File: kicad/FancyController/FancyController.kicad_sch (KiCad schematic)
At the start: 9 parts, among them J3 ISP, U1 ATmega48-20P, U2 MAX232

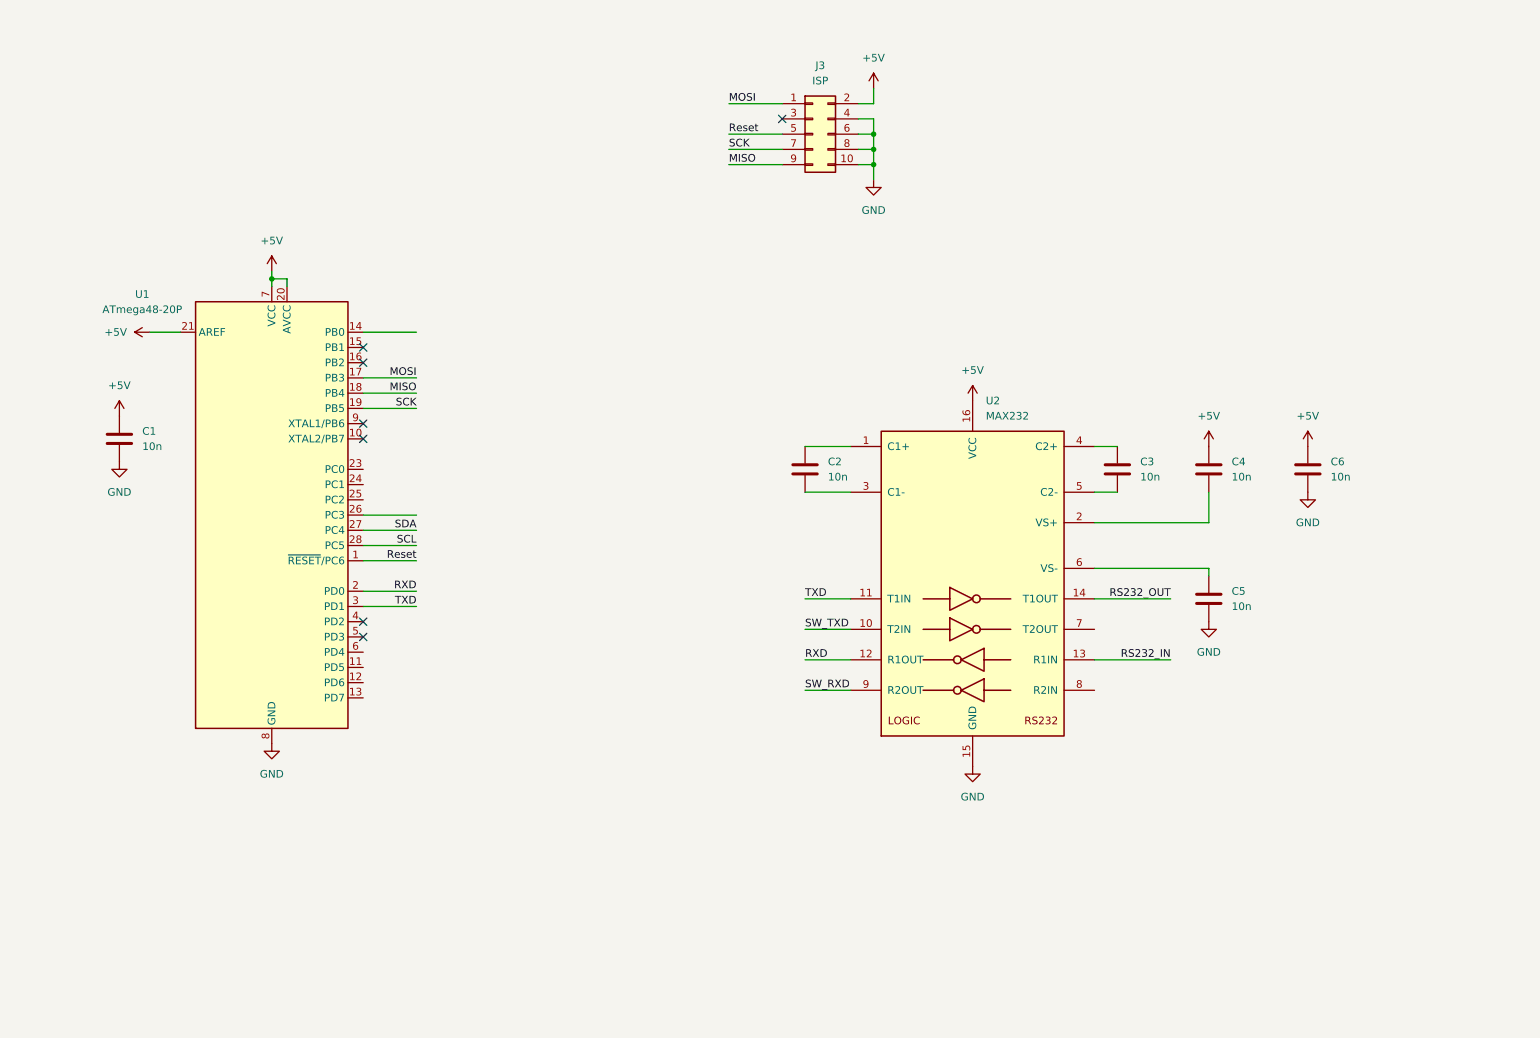
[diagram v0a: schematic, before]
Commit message: Complete schematics, using UART for communications
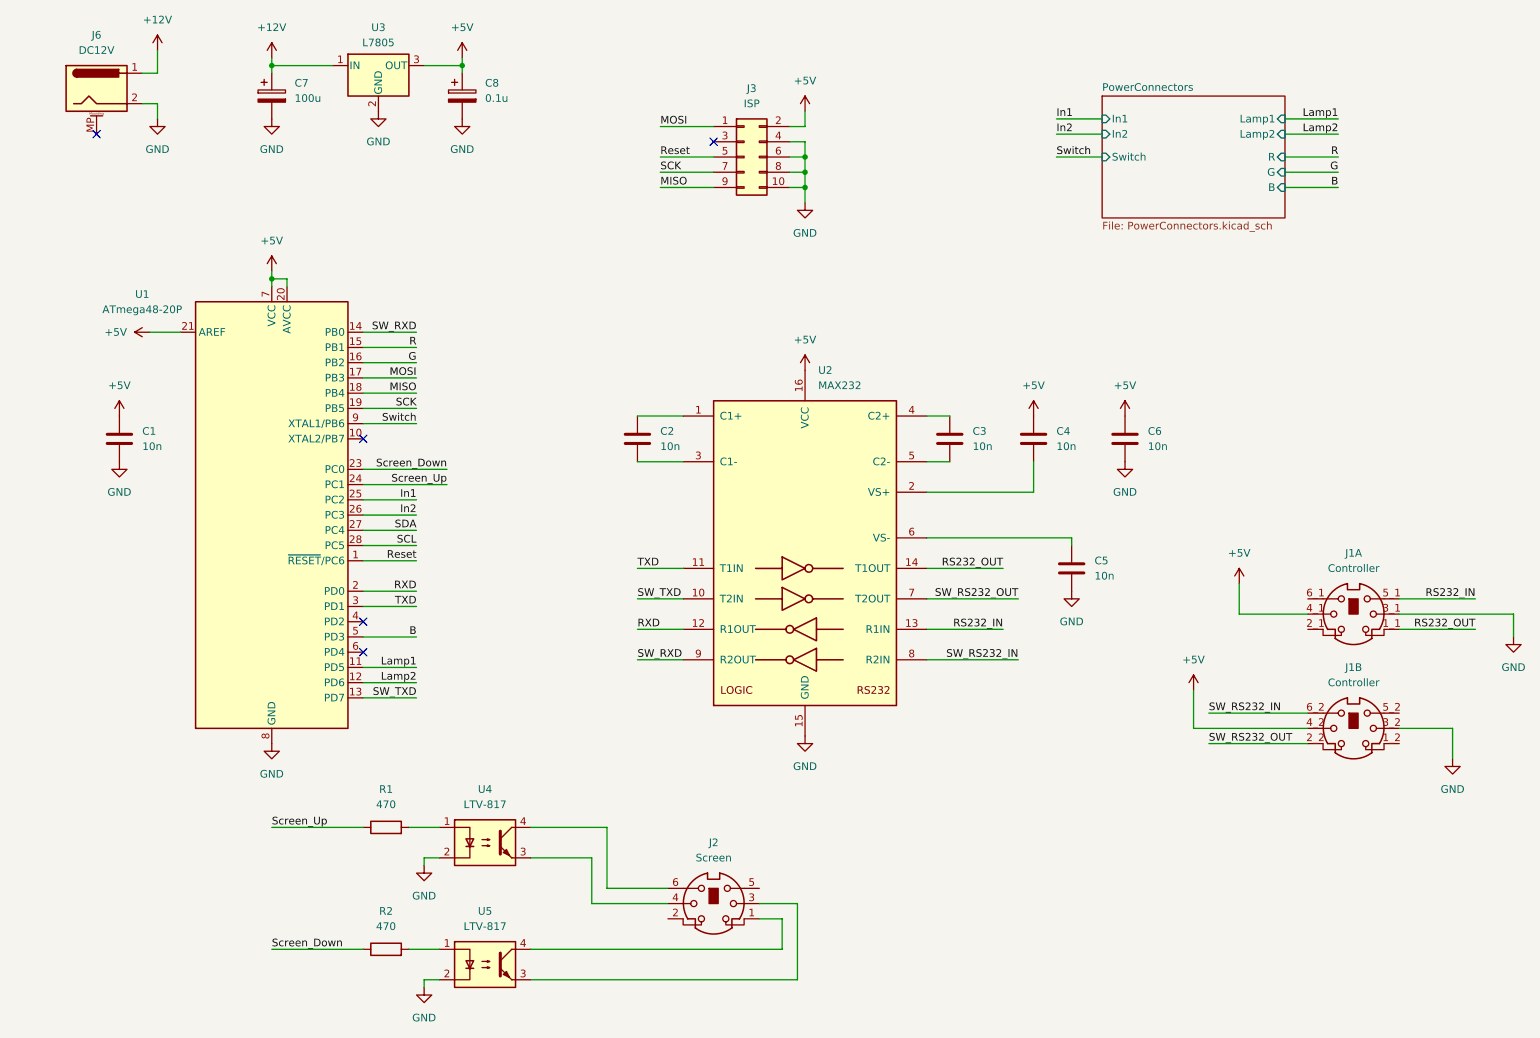
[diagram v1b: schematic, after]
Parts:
- added C7: 100u, symbol Device:C_Polarized
- added C8: 0.1u, symbol Device:C_Polarized
- added J1: Controller, symbol Custom_Symbols:Mini-DIN-2x6
- added J2: Screen, symbol Connector:Mini-DIN-6
- added J6: DC12V, Connector_BarrelJack:BarrelJack_Horizontal, symbol Connector:Barrel_Jack_MountingPin
- added R1, R2: 470, Resistor_THT:R_Axial_DIN0204_L3.6mm_D1.6mm_P2.54mm_Vertical, symbol Device:R
- added U3: L7805, Package_TO_SOT_THT:TO-220-3_Vertical, symbol Regulator_Linear:L7805
- added U4, U5: LTV-817, Package_DIP:DIP-4_W7.62mm, symbol Isolator:LTV-817
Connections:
- net +5V: now also C8.1, J1.4_1, J1.4_2, U3.3 (OUT)
- net GND: now also C7.2, C8.2, J1.3_1, J1.3_2, J6.2, U3.2 (GND), U4.2, U5.2
- net RS232_IN: now also J1.5_1
- net RS232_OUT: now also J1.1_1
- net SW_RXD: now also U1.14 (PB0)
- net SW_TXD: now also U1.13 (PD7)
- net SW_RS232_OUT: now reaches U2.7 (T2OUT)
- net SW_RS232_OUT: now also J1.2_2
- net SW_RS232_IN: now reaches U2.8 (R2IN)
- net SW_RS232_IN: now also J1.6_2
- net Lamp1: now reaches U1.11 (PD5)
- net Lamp2: now reaches U1.12 (PD6)
- net R: now reaches U1.15 (PB1)
- net G: now reaches U1.16 (PB2)
- net Screen_Down: now reaches U1.23 (PC0)
- net Screen_Down: now also R2.1
- net Screen_Up: now reaches U1.24 (PC1)
- net Screen_Up: now also R1.1
- net In1: now reaches U1.25 (PC2)
- net In2: now reaches U1.26 (PC3)
- net B: now reaches U1.5 (PD3)
- net Switch: now reaches U1.9 (XTAL1/PB6)
- new net: R2.2, U5.1
- new net: J2.3, U5.3
- new net: J2.1, U5.4
- new net: R1.2, U4.1
- new net: J2.4, U4.3
- new net: J2.6, U4.4
- new net +12V: C7.1, J6.1, U3.1 (IN)
- no-connect marks 7 -> 5
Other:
- added sheet PowerConnectors (PowerConnectors.kicad_sch)
- moved on the sheet: C2, C3, C4, C5, C6, J3, U2

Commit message: Changed RS232 pin mapping
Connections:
- net SW_RXD: now also U1.10 (XTAL2/PB7); no longer U1.14 (PB0)
- net SW_TXD: now also U1.14 (PB0); no longer U1.13 (PD7)
- net SCL: no longer names the net of U1.28 (PC5)
- net SDA: no longer names the net of U1.27 (PC4)
- no-connect marks 5 -> 13
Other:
- moved on the sheet: J6
